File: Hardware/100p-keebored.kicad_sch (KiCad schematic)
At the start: 28 parts, among them J1 AVR-ISP-6, J2 USB_C_Receptacle_USB2.0, J3 Type C 31-M-12, J4 Conn_01x04, SW130 RotaryEncoder_Switch, SW200 SW_Push, U1 AT90USB1286-A, Y1 JYJE 3TJ480000JYLBC

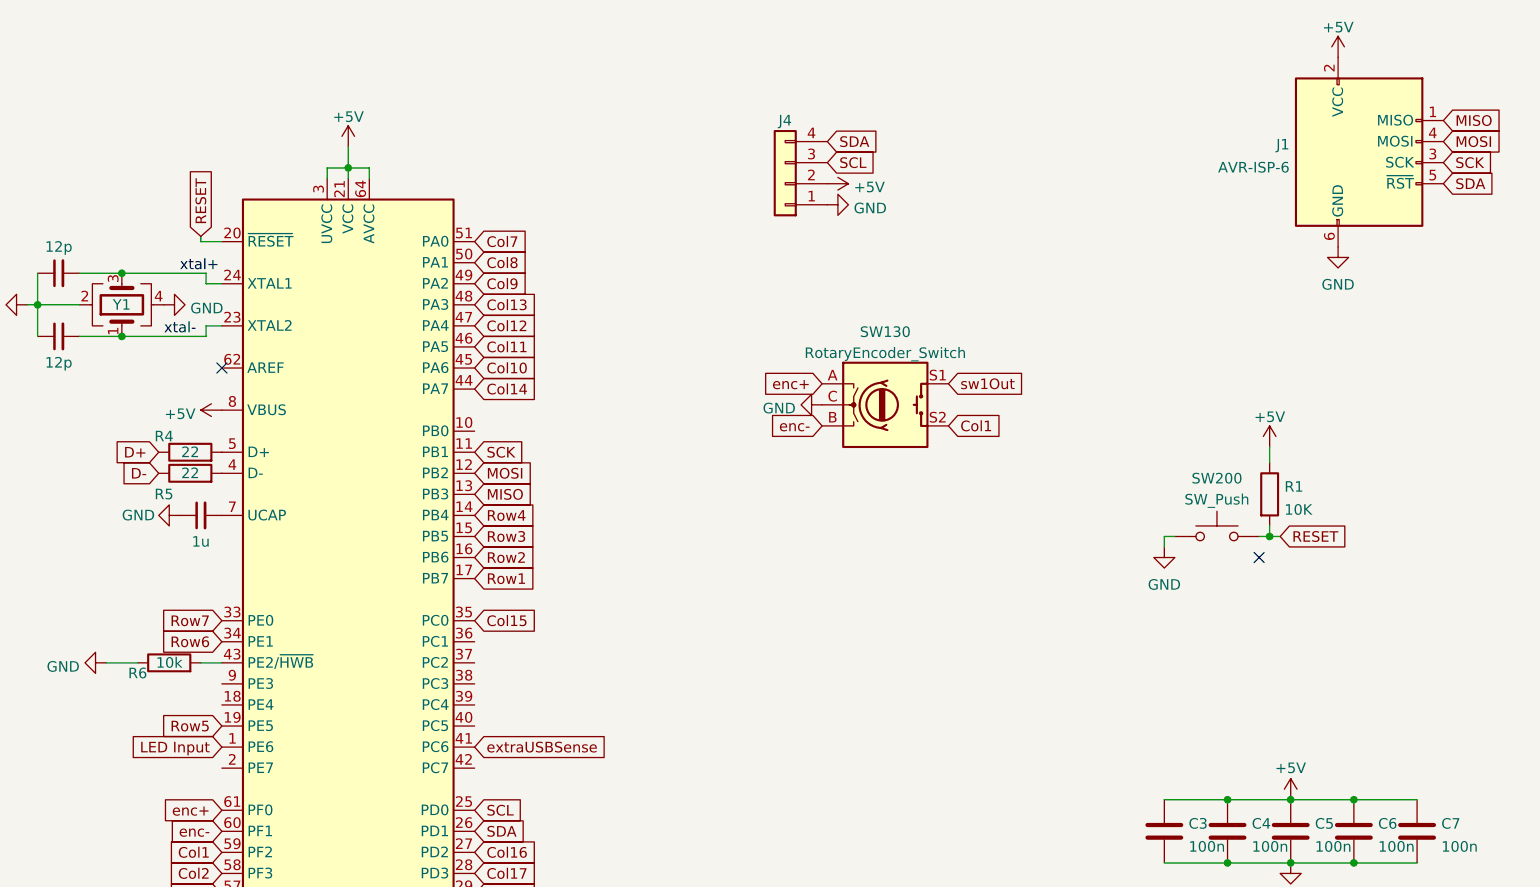
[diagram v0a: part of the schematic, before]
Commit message: general layout complete. trace routing and minir tweaks remain
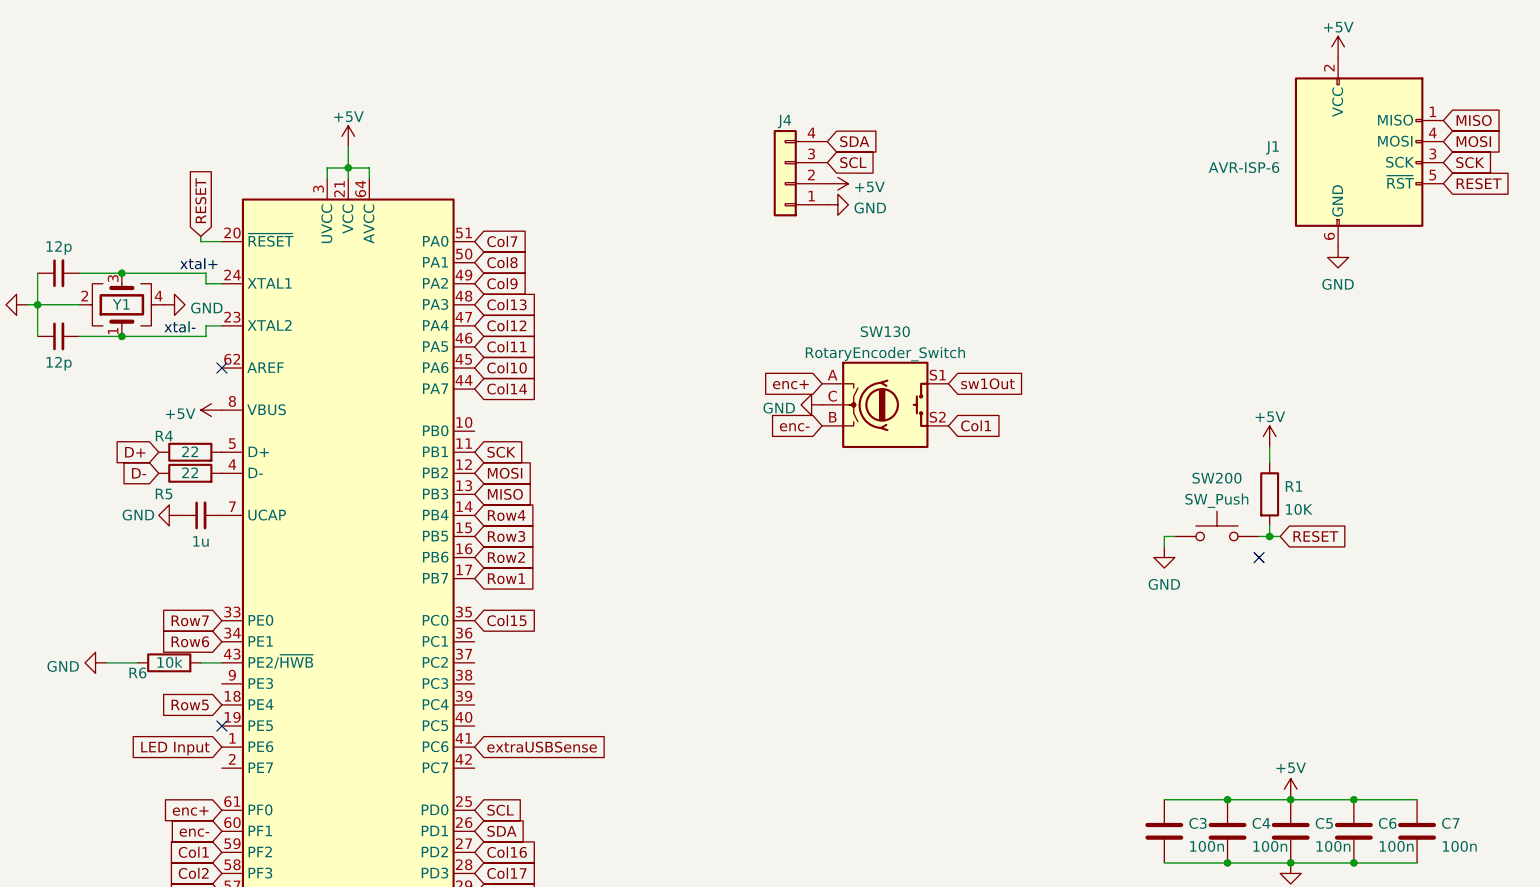
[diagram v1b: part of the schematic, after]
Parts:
- J1: footprint Connector_PinHeader_2.54mm:PinHeader_2x03_P2.54mm_Vertical -> Connector:Tag-Connect_TC2030-IDC-NL_2x03_P1.27mm_Vertical
- J4: footprint Display:SSD1306 128x32 -> SSD1306:SSD1306_128_32
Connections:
- net RESET: now also J1.5 (~{RST})
- net Row5: now also U1.18 (PE4); no longer U1.19 (PE5)
- net SDA: no longer J1.5 (~{RST})
- no-connect marks 12 -> 13
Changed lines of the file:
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@@
   (no_connect (at 45.72 131.445))
   (no_connect (at 45.72 133.985))
+  (no_connect (at 126.365 100.965))
   (no_connect (at 43.18 72.39))
   (no_connect (at 43.18 74.93))
@@
     )
   )
-  (global_label "Row5" (shape input) (at 126.365 100.965 180) (fields_autoplaced)
-    (effects (font (size 1.27 1.27)) (justify right))
-    (property "Intersheetrefs" "${INTERSHEET_REFS}" (at 118.9929 100.8856 0)
+  (global_label "Row5" (shape input) (at 126.365 98.425 180) (fields_autoplaced)
+    (effects (font (size 1.27 1.27)) (justify right))
+    (property "Intersheetrefs" "${INTERSHEET_REFS}" (at 118.9929 98.3456 0)
       (effects (font (size 1.27 1.27)) (justify right) hide)
     )
@@
     )
   )
-  (global_label "SDA" (shape input) (at 273.685 35.56 0) (fields_autoplaced)
-    (effects (font (size 1.27 1.27)) (justify left))
-    (property "Intersheetrefs" "${INTERSHEET_REFS}" (at 279.6662 35.4806 0)
-      (effects (font (size 1.27 1.27)) (justify left) hide)
-    )
-  )
   (global_label "Col20" (shape input) (at 156.845 126.365 0) (fields_autoplaced)
     (effects (font (size 1.27 1.27)) (justify left))
@@
     (effects (font (size 1.27 1.27)) (justify left))
     (property "Intersheetrefs" "${INTERSHEET_REFS}" (at 164.2171 80.7244 0)
+      (effects (font (size 1.27 1.27)) (justify left) hide)
+    )
+  )
+  (global_label "RESET" (shape input) (at 273.685 35.56 0) (fields_autoplaced)
+    (effects (font (size 1.27 1.27)) (justify left))
+    (property "Intersheetrefs" "${INTERSHEET_REFS}" (at 282.3359 35.56 0)
       (effects (font (size 1.27 1.27)) (justify left) hide)
     )
@@
   (symbol (lib_id "Connector:AVR-ISP-6") (at 263.525 33.02 0) (unit 1)
     (in_bom yes) (on_board yes) (dnp no) (fields_autoplaced)
-    (property "Reference" "J1" (at 255.1431 30.8415 0)
+    (property "Reference" "J1" (at 254 31.115 0)
       (effects (font (size 1.27 1.27)) (justify right))
     )
-    (property "Value" "AVR-ISP-6" (at 255.1431 33.6166 0)
+    (property "Value" "AVR-ISP-6" (at 254 33.655 0)
       (effects (font (size 1.27 1.27)) (justify right))
     )
-    (property "Footprint" "Connector_PinHeader_2.54mm:PinHeader_2x03_P2.54mm_Vertical" (at 257.175 31.75 90)
+    (property "Footprint" "Connector:Tag-Connect_TC2030-IDC-NL_2x03_P1.27mm_Vertical" (at 257.175 31.75 90)
       (effects (font (size 1.27 1.27)) hide)
     )
@@
       (effects (font (size 1.27 1.27)) hide)
     )
-    (property "Footprint" "Display:SSD1306 128x32" (at 194.31 35.56 0)
-      (effects (font (size 1.27 1.27)) hide)
-    )
+    (property "Footprint" "SSD1306:SSD1306_128_32" (at 194.31 35.56 0)
+      (effects (font (size 1.27 1.27)) hide)
+    )

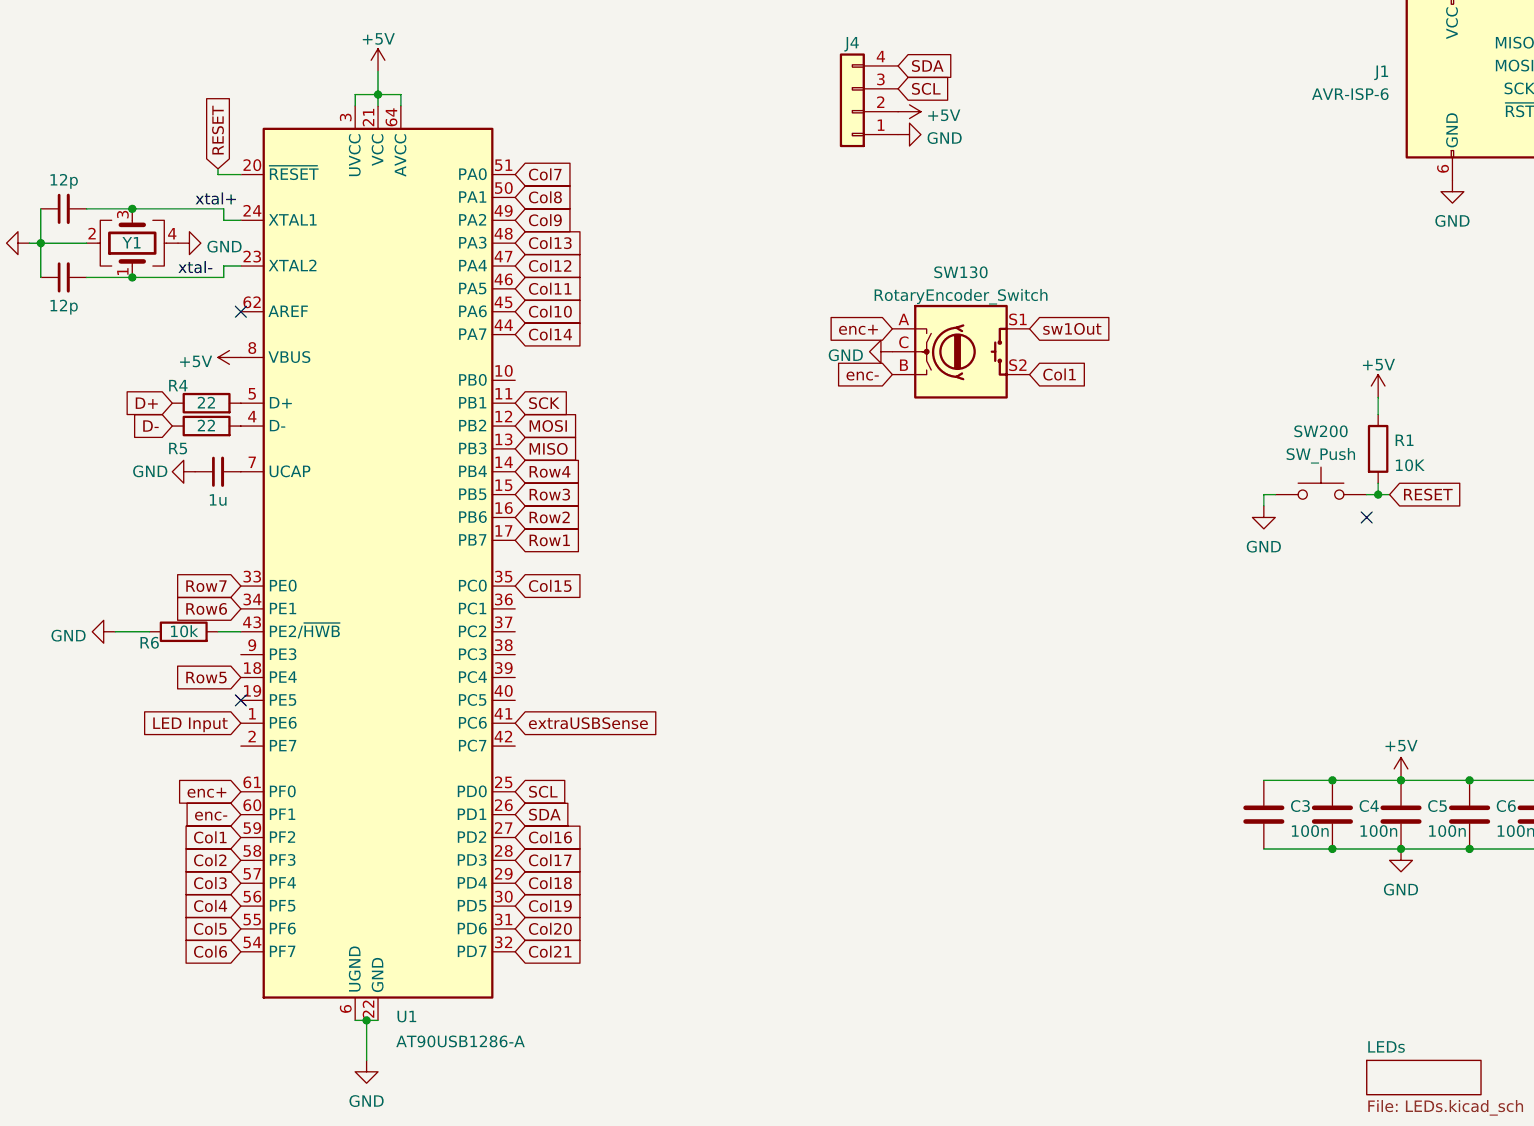
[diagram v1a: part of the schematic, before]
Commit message: Massive Progress
- Completed general layout. I believe this should function as a full keyboard.

- Missing Caps/Num/Scroll Lock Indicators (LEDS). OLED can take this up, but should we look into adding these? If so, where?

- Tempted to add a second optional encoder to the top right of the board as well.

- All I can think of at the moment, but there may be more.
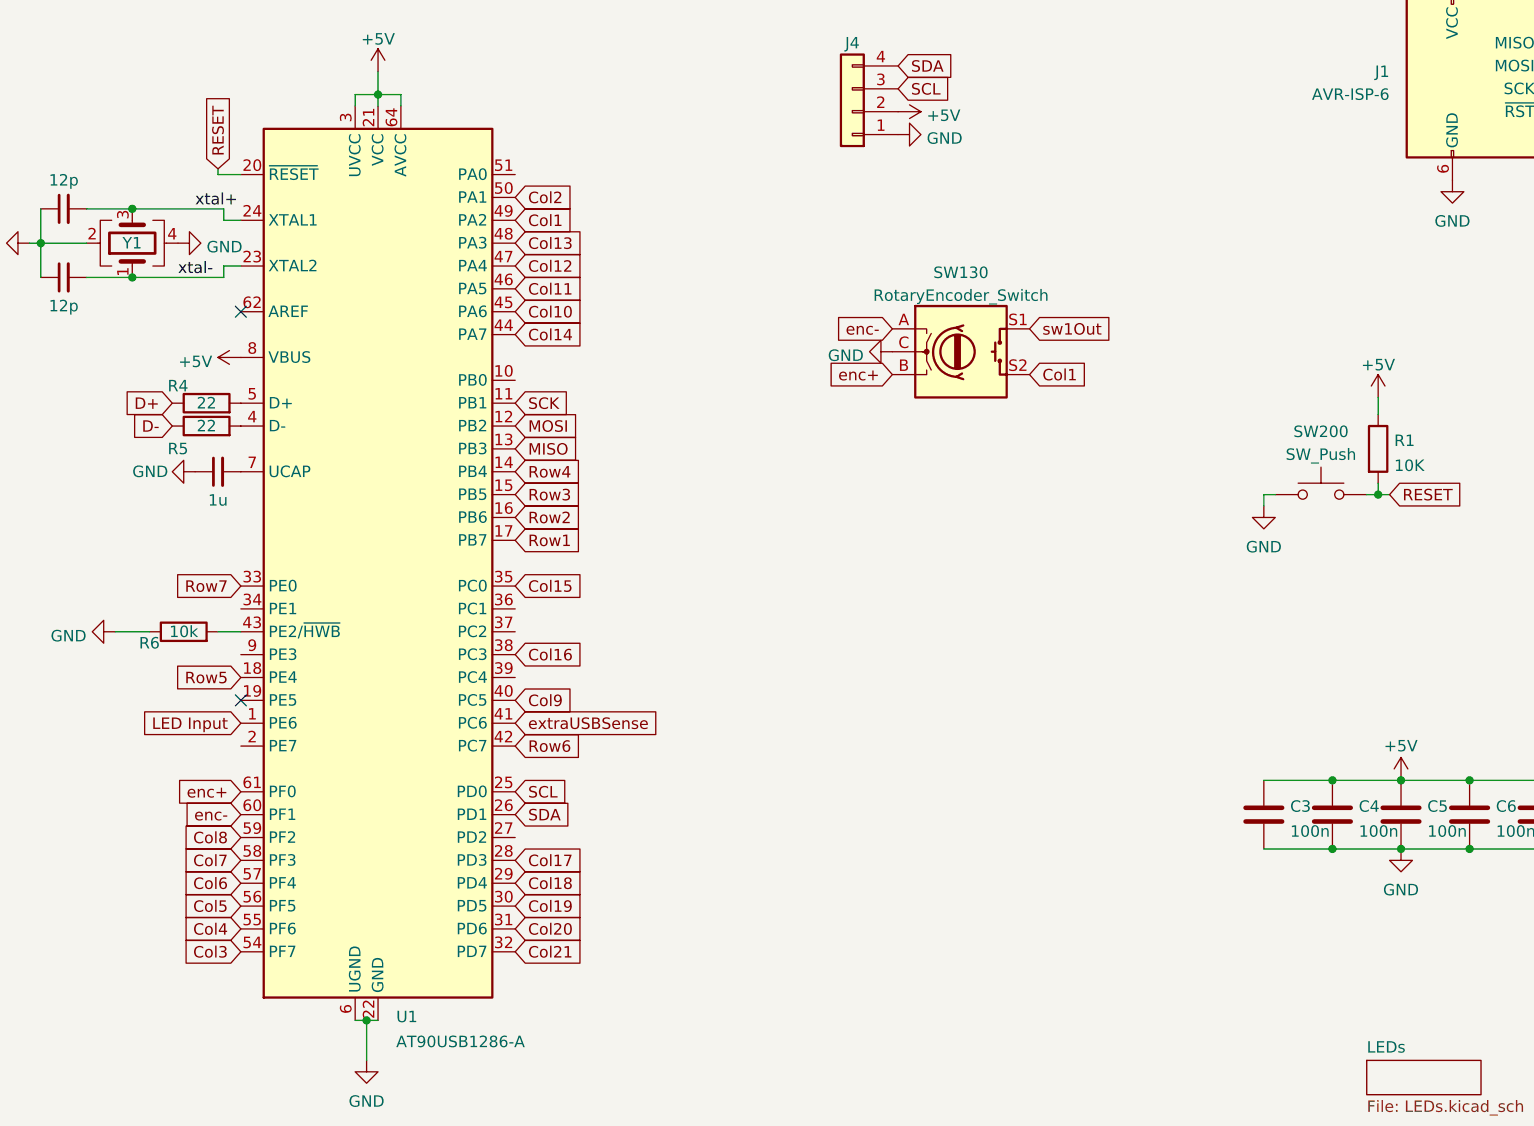
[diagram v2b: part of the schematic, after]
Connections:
- net Col1: now also U1.49 (PA2); no longer U1.59 (PF2)
- net Col16: now also U1.38 (PC3); no longer U1.27 (PD2)
- net Col2: now also U1.50 (PA1); no longer U1.58 (PF3)
- net Col3: now also U1.54 (PF7); no longer U1.57 (PF4)
- net Col4: now also U1.55 (PF6); no longer U1.56 (PF5)
- net Col5: now also U1.56 (PF5); no longer U1.55 (PF6)
- net Col6: now also U1.57 (PF4); no longer U1.54 (PF7)
- net Col7: now also U1.58 (PF3); no longer U1.51 (PA0)
- net Col8: now also U1.59 (PF2); no longer U1.50 (PA1)
- net Col9: now also U1.40 (PC5); no longer U1.49 (PA2)
- net Row6: now also U1.42 (PC7); no longer U1.34 (PE1)
- net enc+: now also SW130.B; no longer SW130.A
- net enc-: now also SW130.A; no longer SW130.B
- no-connect marks 13 -> 12

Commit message: Final design for v2.0
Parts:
- removed D130: SBRT5A50SA-13, Diode_SMD:D_SMA, symbol pspice:DIODE
- removed D131: BZT52C5V6, Diode_SMD:D_SOD-123, symbol Device:D_Zener
- removed F1: JFC0402-0250FS, Fuse:Fuse_0402_1005Metric, symbol Device:Polyfuse
- added D130: PRTR5V0U2X, Package_TO_SOT_SMD:SOT-143, symbol Power_Protection:PRTR5V0U2X
- added R9: 10k, Resistor_SMD:R_0402_1005Metric, symbol Device:R
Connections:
- net +5V: now also J3.A4 (VBUS), J3.A9 (VBUS), J3.B4 (VBUS), J3.B9 (VBUS), D130.4 (VCC), R9.2
- net GND: now also J2.S1 (SHIELD), J3.S1 (SHIELD), D130.1 (GND)
- net A+: now reaches J3.A6 (D+)
- net A+: now also J3.B6 (D+), D130.2 (I/O1)
- net A-: now reaches J3.A7 (D-)
- net A-: now also J3.B7 (D-), D130.3 (I/O2)
- net extraUSBSense: no longer names the net of U1.41 (PC6)
- net extraUSBSense: now also R9.1
- no-connect marks 12 -> 6
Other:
- note added: "AT90USB1286 MCU"
- note added: "AUX Power In ESD Protection Sense"
- note added: "Encoder"
- note added: "ISP Header"
- note added: "OLED Display SSD1306 128x32"
- note added: "Power Filtering"
- note added: "Reset Switch Bootloader Mode"
- note added: "USB Data + Power IN"
- note added: "USB ESD Protection"
- moved on the sheet: C3, C4, C5, C6, C7, D200, J1, J2, J3, J4, R1, R2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

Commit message: Increment to Rev 2.1, Fix Lock Indicators, Repair Ground Connection D280, move covered mount hole.
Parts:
- R2, R3, R7, R8: value 5.1k -> 5k1
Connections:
- no-connect marks 6 -> 15
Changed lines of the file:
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@@
   (no_connect (at 39.37 160.655))
   (no_connect (at 39.37 163.195))
+  (no_connect (at 156.845 78.74))
+  (no_connect (at 156.845 53.34))
+  (no_connect (at 156.845 81.28))
   (no_connect (at 126.365 88.9))
+  (no_connect (at 126.365 93.98))
   (no_connect (at 41.275 52.705))
   (no_connect (at 41.275 55.245))
+  (no_connect (at 156.845 30.48))
   (no_connect (at 126.365 45.72))
+  (no_connect (at 126.365 83.82))
+  (no_connect (at 126.365 78.74))
+  (no_connect (at 156.845 86.36))
+  (no_connect (at 156.845 104.14))
   (wire (pts (xy 123.825 81.28) (xy 126.365 81.28))
     (stroke (width 0) (type default))
@@
   (symbol (lib_id "Device:R_Small") (at 43.815 137.795 90) (unit 1)
     (in_bom yes) (on_board yes) (dnp no)
-    (property "Reference" "R7" (at 43.815 137.795 90)
-      (effects (font (size 1.27 1.27)))
-    )
-    (property "Value" "5.1k" (at 41.91 142.24 90)
+    (property "Reference" "R7" (at 43.815 135.89 90)
+      (effects (font (size 1.27 1.27)))
+    )
+    (property "Value" "5k1" (at 43.815 140.335 90)
       (effects (font (size 1.27 1.27)))
     )
@@
       (effects (font (size 1.27 1.27)))
     )
-    (property "Value" "5.1k" (at 46.355 32.385 90)
+    (property "Value" "5k1" (at 46.355 32.385 90)
       (effects (font (size 1.27 1.27)))
     )
@@
   (symbol (lib_id "Device:R_Small") (at 43.815 140.335 90) (unit 1)
     (in_bom yes) (on_board yes) (dnp no)
-    (property "Reference" "R8" (at 43.815 140.335 90)
-      (effects (font (size 1.27 1.27)))
-    )
-    (property "Value" "5.1k" (at 41.91 135.89 90)
+    (property "Reference" "R8" (at 43.815 142.24 90)
+      (effects (font (size 1.27 1.27)))
+    )
+    (property "Value" "5k1" (at 43.815 137.795 90)
       (effects (font (size 1.27 1.27)))
     )
@@
       (effects (font (size 1.27 1.27)))
     )
-    (property "Value" "5.1k" (at 46.355 29.845 90)
-      (effects (font (size 1.27 1.27)))
-    )
+    (property "Value" "5k1" (at 46.355 29.845 90)
+      (effects (font (size 1.27 1.27)))
+    )
